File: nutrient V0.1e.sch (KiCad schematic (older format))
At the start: 76 parts, among them J1 Conn_01x04_Female, J10 Conn_01x01_Male, J2 Conn_01x04_Female, J3 Conn_01x04_Female, J4 Conn_01x04_Female, J5 Conn_01x04_Female, J6 Conn_01x04_Female, J7 Conn_01x03_Male, J8 Conn_01x03_Male, J9 Conn_01x01_Male, P1 SolderJumper_2_Open, P2 SolderJumper_2_Bridged, Q1 Q_NMOS_DGS, Q10 Q_NMOS_DGS, Q2 Q_NMOS_DGS, Q3 Q_NMOS_DGS, Q4 Q_NMOS_DGS, Q5 Q_NMOS_DGS, Q6 Q_NMOS_DGS, Q7 Q_NMOS_DGS, Q8 2N3904, U1 23LC512, U2 DS1307+, Y1 Crystal_Small

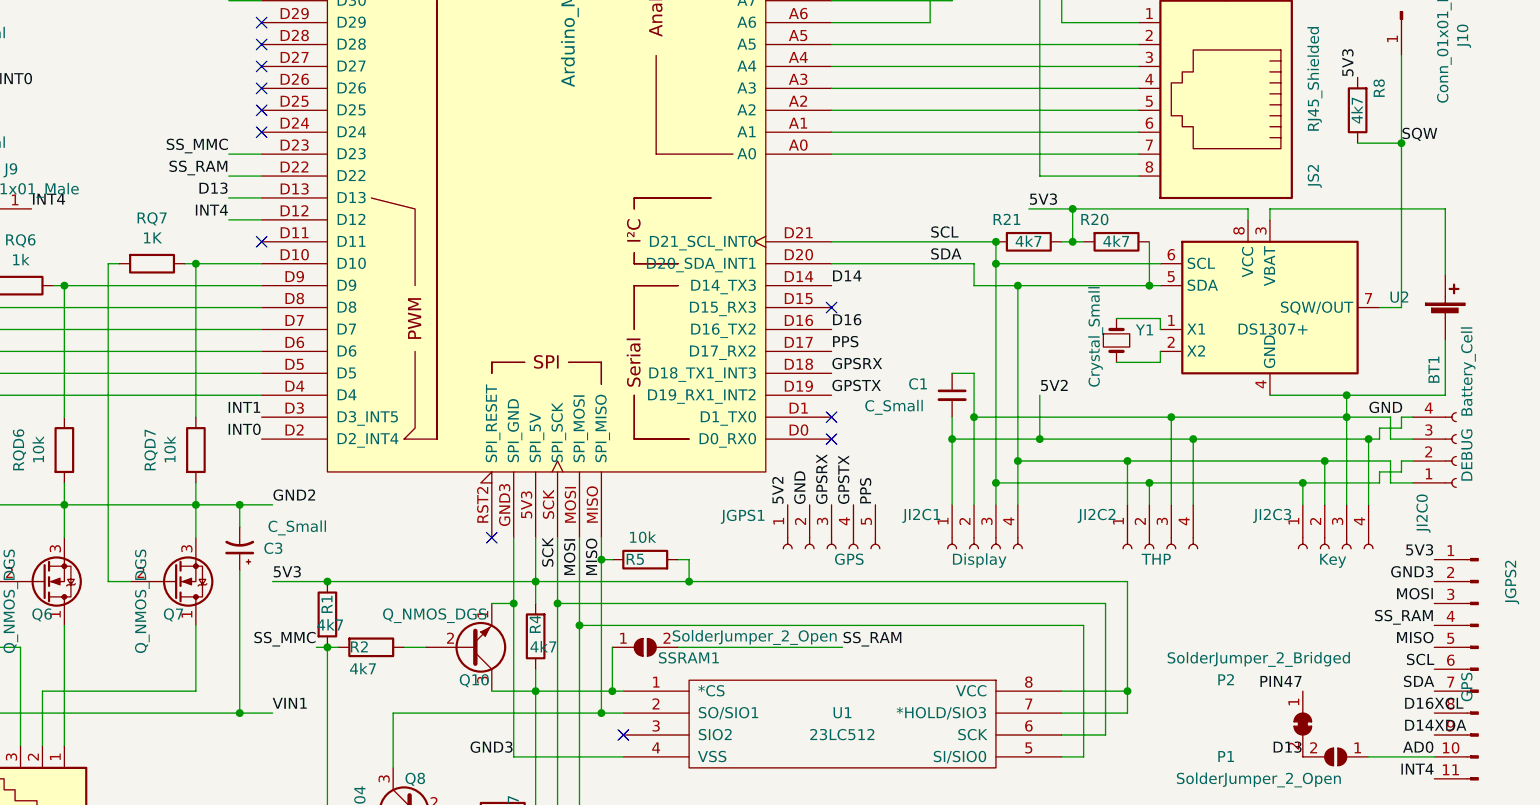
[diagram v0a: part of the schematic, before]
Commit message: Minor track changes
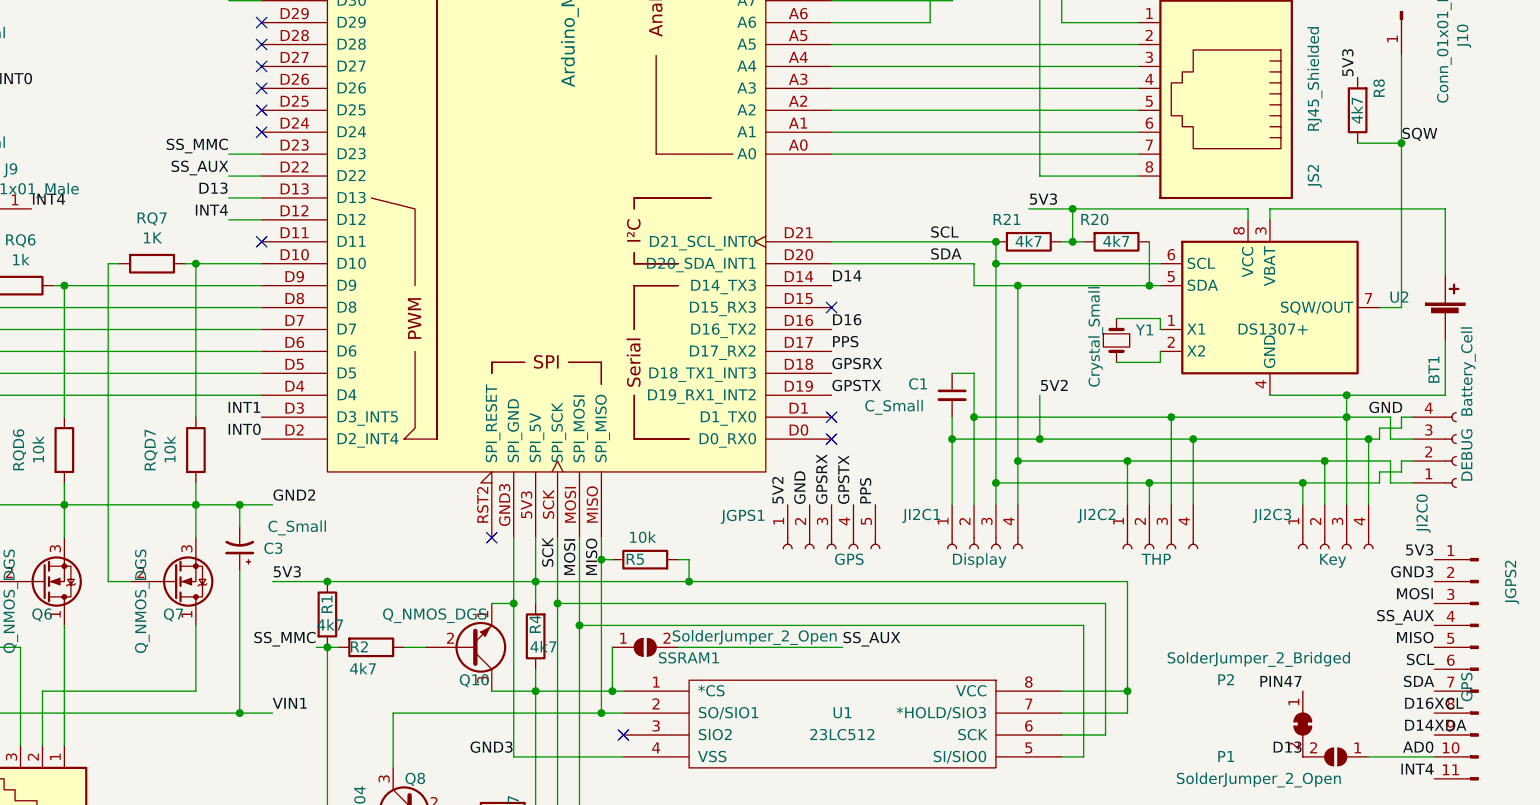
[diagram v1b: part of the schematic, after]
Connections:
- net SS_RAM renamed SS_AUX
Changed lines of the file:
@@
 Connection ~ 6850 5800
 Text Label 5250 3750 2    50   ~ 0
-SS_RAM
+SS_AUX
 Wire Wire Line
 	6850 5800 6850 7200
@@
 $EndComp
 Text Label 8050 5900 0    50   ~ 0
-SS_RAM
+SS_AUX
 $Comp
 L Jumper:SolderJumper_2_Open SSRAM1
@@
 SCL
 Text Label 10750 5800 2    50   ~ 0
-SS_RAM
+SS_AUX
 Text Label 10750 5900 2    50   ~ 0
 MISO
